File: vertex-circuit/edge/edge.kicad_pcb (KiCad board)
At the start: 2 copper layers, 50 x 100 mm, 4 parts

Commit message: legit circuit!
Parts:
- moved ARM_1 40.9 mm to (150.0, 120.0), turned to 270 degrees
- moved ARM_2 40.9 mm to (132.7, 90.0), turned to 330 degrees
- moved ARM_3 7.00 mm to (167.3, 90.0)
- turned IO to 270 degrees
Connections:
- net ARM_2_TO_ARM_3_CLOCK renamed ARM_2_CLOCK_TO_ARM_3_CLOCK
- net ARM_2_TO_ARM_3_DATA renamed ARM_2_DATA_TO_ARM_3_DATA
- net IO_TO_ARM_1_CLOCK renamed IO_CLOCK_TO_ARM_1_CLOCK
- net IO_TO_ARM_1_DATA renamed IO_DATA_TO_ARM_1_DATA
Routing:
- net GND: track 0.00 -> 50.8 mm
- net +5V: track 0.00 -> 49.6 mm
- net ARM_2_CLOCK_TO_ARM_3_CLOCK: track 0.00 -> 35.9 mm
- net ARM_2_DATA_TO_ARM_3_DATA: track 0.00 -> 33.4 mm
- net IO_DATA_TO_ARM_1_DATA: track 0.00 -> 20.0 mm
- net IO_CLOCK_TO_ARM_1_CLOCK: track 0.00 -> 20.0 mm
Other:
- board size 50 x 100 mm -> 60.6 x 52.5 mm
- net class Power: trace_width 1 -> 1.4; via_dia 1.2 -> 1.4

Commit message: checkpoint
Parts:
- removed the IO at (150.0, 100.0)
- added IO: H4-2.54mm, H4-2.54mm, F.Cu at (150.0, 100.0)
- ARM_1, ARM_2, ARM_3: footprint PinHeader_1x04_P2.54mm_Vertical_Centered -> H4-2.54mm
- moved ARM_1 35.0 mm to (150.0, 85.0)
- moved ARM_3 18.0 mm to (163.0, 107.5), turned to 150 degrees
- moved ARM_2 18.0 mm to (137.0, 107.5), turned to 210 degrees
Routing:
- net GND: track 50.8 -> 0.00 mm
- net +5V: track 49.6 -> 0.00 mm
- net ARM_2_CLOCK_TO_ARM_3_CLOCK: track 35.9 -> 0.00 mm
- net ARM_2_DATA_TO_ARM_3_DATA: track 33.4 -> 0.00 mm
- net IO_DATA_TO_ARM_1_DATA: track 20.0 -> 0.00 mm
- net IO_CLOCK_TO_ARM_1_CLOCK: track 20.0 -> 0.00 mm
- added copper zone on F.Cu, net GND
- removed copper zone on B.Cu, net GND
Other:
- board size 60.6 x 52.5 mm -> 40 x 34.6 mm
- net class Power: clearance 0.254 -> 0.5; trace_width 1.4 -> 1.7; via_dia 1.4 -> 1.7; via_drill 0.635 -> 0.8

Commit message: hey hey we can generate the entire circuit board meow!
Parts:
- removed ARM_1, ARM_2, ARM_3, IO: H4-2.54mm, H4-2.54mm
- added J1: IO, H4-2.54mm,  at (150.0, 100.0)
- added J2: ARM_1, H4-2.54mm,  at (150.0, 85.0)
- added J3: ARM_2, H4-2.54mm,  at (137.0, 107.5)
- added J4: ARM_3, H4-2.54mm,  at (163.0, 107.5)
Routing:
- net +5V: track 0.00 -> 37.9 mm
- net GND: track 0.00 -> 37.2 mm
- net ARM_2_CLOCK_TO_ARM_3_CLOCK: track 0.00 -> 27.3 mm
- net ARM_2_DATA_TO_ARM_3_DATA: track 0.00 -> 24.7 mm
- net IO_DATA_TO_ARM_1_DATA: track 0.00 -> 15.0 mm
- net IO_CLOCK_TO_ARM_1_CLOCK: track 0.00 -> 15.0 mm
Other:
- net class Power: trace_width 1.7 -> 1.6; via_dia 1.7 -> 1.6

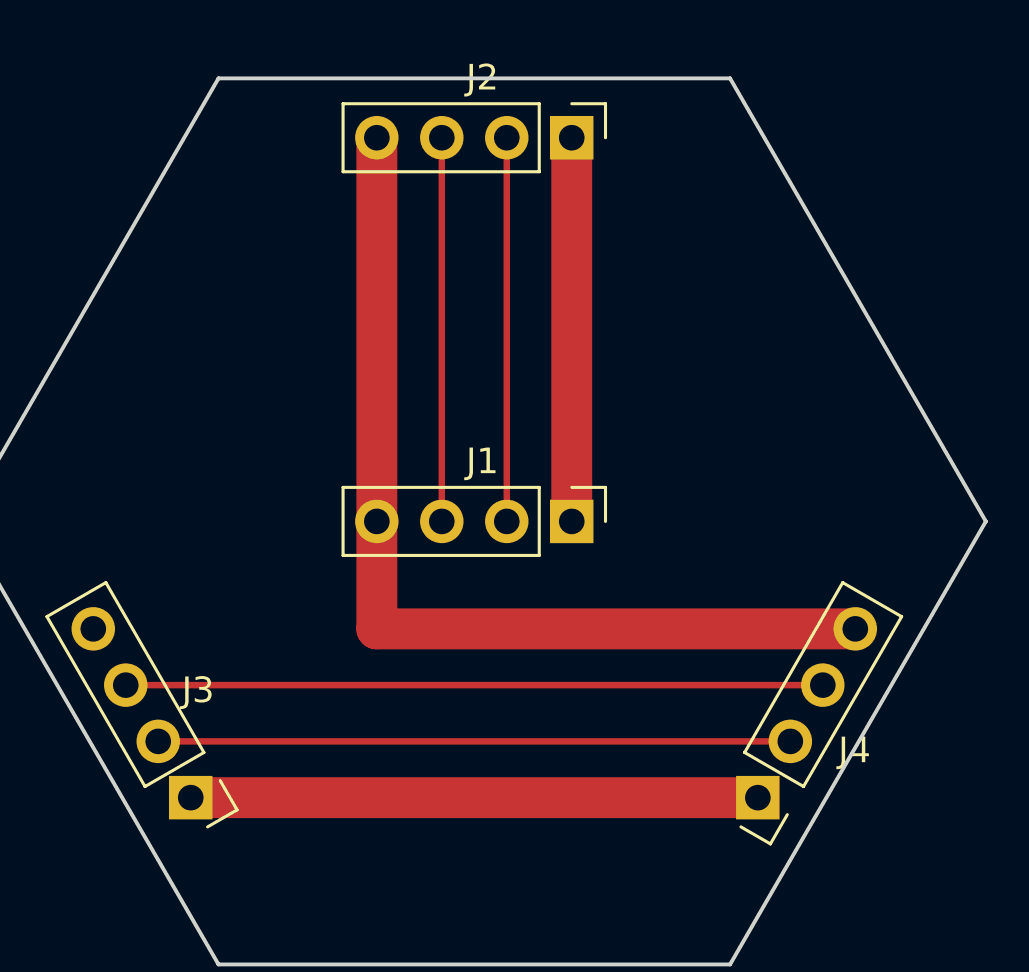
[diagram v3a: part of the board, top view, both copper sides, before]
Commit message: add some mounting screws, tiny fixes
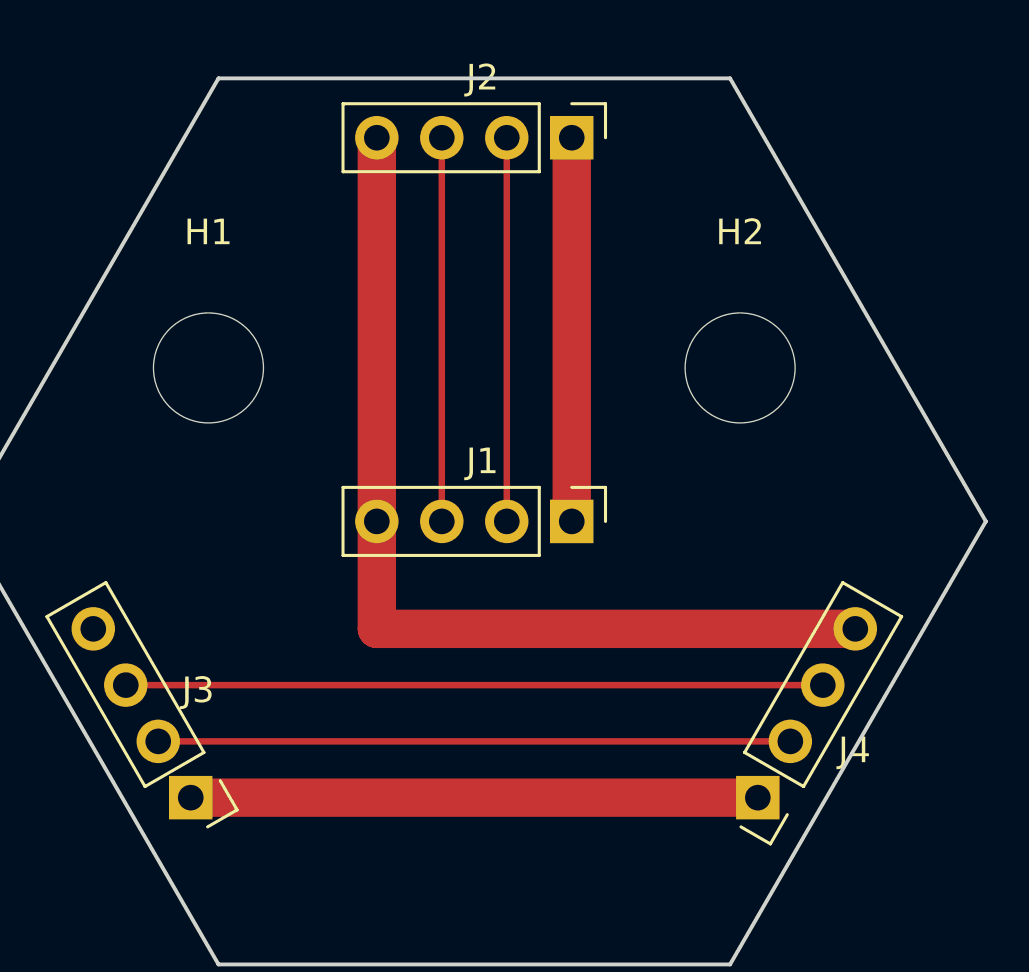
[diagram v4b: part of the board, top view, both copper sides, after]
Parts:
- added H1: M4, M4,  at (139.6, 94.0)
- added H2: M4, M4,  at (160.4, 94.0)
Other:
- net class Power: clearance 0.5 -> 0.4; trace_width 1.6 -> 1.5; via_dia 1.6 -> 1.5
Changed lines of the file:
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@@
   (host
     pcbnew
-    jseda-2.0.0
+    jseda-2.0.1
   )
   (general
@@
     (tracks 9)
     (zones 1)
-    (modules 4)
+    (modules 6)
     (nets 8)
   )
@@
     Power
     "net class for high-power"
-    (clearance 0.5)
-    (trace_width 1.6)
-    (via_dia 1.6)
+    (clearance 0.4)
+    (trace_width 1.5)
+    (via_dia 1.5)
     (via_drill 0.8)
-    (uvia_dia 1.6)
+    (uvia_dia 1.5)
     (uvia_drill 0.8)
     (add_net +5V)
@@
     )
   )
+  (module
+    M4
+    (at
+      139.60769515458674
+      94
+    )
+    (descr "Mounting Hole 4.3mm, no annular, M4")
+    (tags "mounting hole 4.3mm no annular m4")
+    (pad
+      1
+      np_thru_hole
+      circle
+      (at
+        0
+        0
+      )
+      (size
+        4.3
+        4.3
+      )
+      (drill 4.3)
+      (layers
+        *.Cu
+        *.Mask
+      )
+      (net
+        2
+        GND
+      )
+    )
+    (fp_text
+      reference
+      H1
+      (at
+        0
+        -5.3
+      )
+      (layer F.SilkS)
+      (effects
+        (font
+          (size
+            1
+            1
+          )
+          (thickness 0.15)
+        )
+      )
+    )
+    (fp_text
+      value
+      M4
+      (at
+        0
+        5.3
+      )
+      (layer F.Fab)
+      (effects
+        (font
+          (size
+            1
+            1
+          )
+          (thickness 0.15)
+        )
+      )
+    )
+    (fp_circle
+      (center
+        0
+        0
+      )
+      (end
+        4.55
+        0
+      )
+      (layer F.CrtYd)
+      (width 0.05)
+    )
+  )
+  (module
+    M4
+    (at
+      160.39230484541326
+      94
+    )
+    (descr "Mounting Hole 4.3mm, no annular, M4")
+    (tags "mounting hole 4.3mm no annular m4")
+    (pad
+      1
+      np_thru_hole
+      circle
+      (at
+        0
+        0
+      )
+      (size
+        4.3
+        4.3
+      )
+      (drill 4.3)
+      (layers
+        *.Cu
+        *.Mask
+      )
+      (net
+        2
+        GND
+      )
+    )
+    (fp_text
+      reference
+      H2
+      (at
+        0
+        -5.3
+      )
+      (layer F.SilkS)
+      (effects
+        (font
+          (size
+            1
+            1
+          )
+          (thickness 0.15)
+        )
+      )
+    )
+    (fp_text
+      value
+      M4
+      (at
+        0
+        5.3
+      )
+      (layer F.Fab)
+      (effects
+        (font
+          (size
+            1
+            1
+          )
+          (thickness 0.15)
+        )
+      )
+    )
+    (fp_circle
+      (center
+        0
+        0
+      )
+      (end
+        4.55
+        0
+      )
+      (layer F.CrtYd)
+      (width 0.05)
+    )
+  )
   (segment
     (start
@@
       85
     )
-    (width 1.6)
+    (width 1.5)
     (layer F.Cu)
     (net
@@
       85
     )
-    (width 1.6)
+    (width 1.5)
     (layer F.Cu)
     (net
@@
       110.79955678841871
     )
-    (width 1.6)
+    (width 1.5)
     (layer F.Cu)
     (net
@@
       104.20044321158129
     )
-    (width 1.6)
+    (width 1.5)
     (layer F.Cu)
     (net
@@
       104.20044321158129
     )
-    (width 1.6)
+    (width 1.5)
     (layer F.Cu)
     (net

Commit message: run drc, save from kicad
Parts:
- H1, H2, J1, J2, J3, J4: moved to F.Cu
